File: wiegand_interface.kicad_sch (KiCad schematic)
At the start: 10 parts, among them U7 LTV-827S, U8 LTV-827S

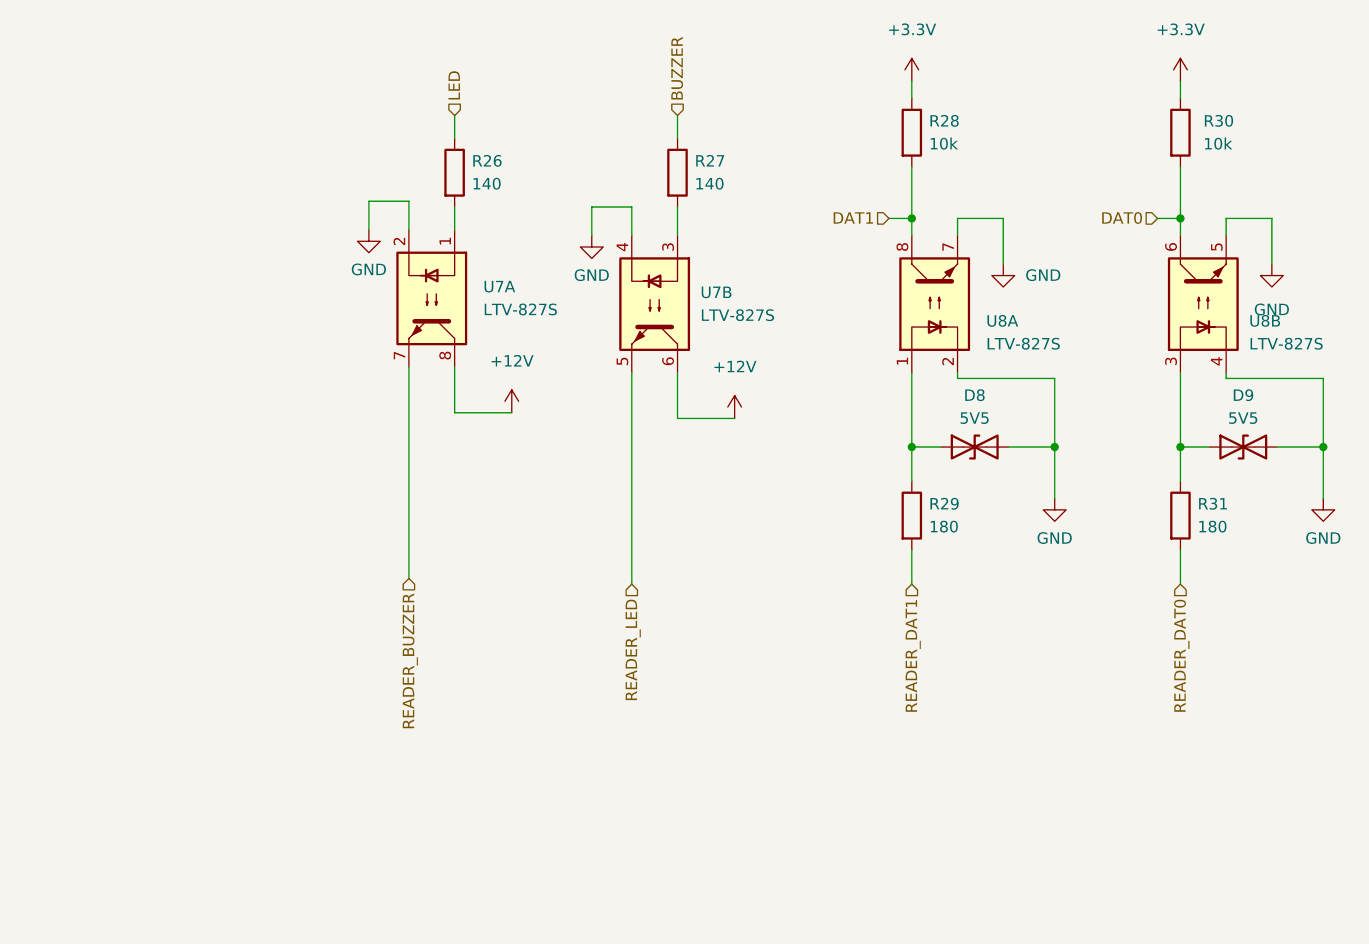
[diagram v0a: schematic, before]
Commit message: fix PoE transofrmer polarity, add more relay outputs
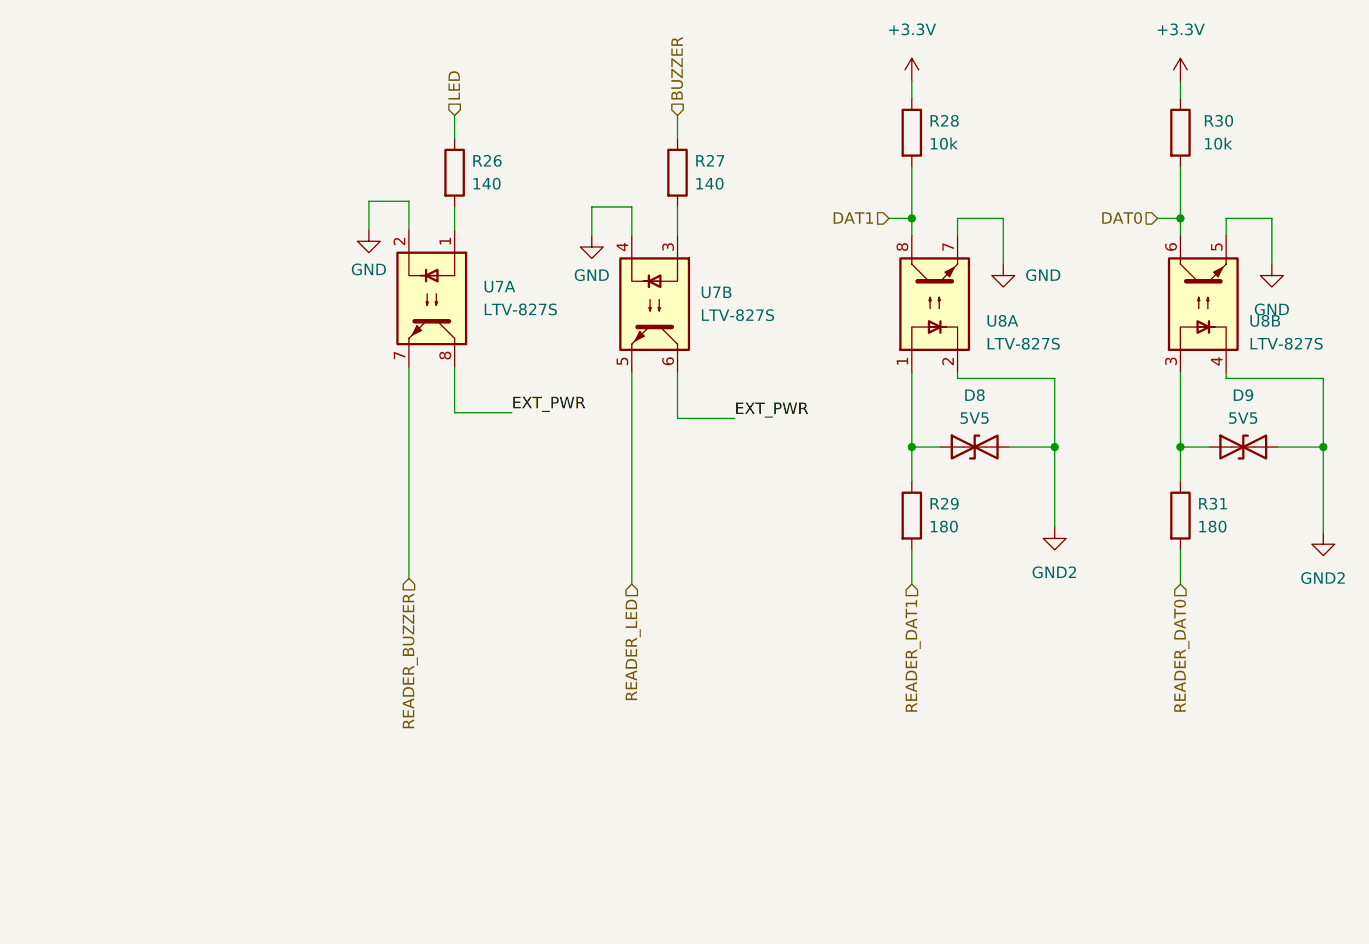
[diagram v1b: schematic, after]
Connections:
- net GND: no longer D8.2 (A2), D9.2 (A2), U8.2, U8.4
- net +12V renamed EXT_PWR
- new net GND2: D8.2 (A2), D9.2 (A2), U8.2, U8.4
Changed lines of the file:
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@@
+	(wire
+		(pts
+			(xy 160.02 114.3) (xy 160.02 123.19)
+		)
+		(stroke
+			(width 0)
+			(type default)
+		)
+	)
 	(wire
 		(pts
@@
 	(wire
 		(pts
-			(xy 160.02 120.015) (xy 160.02 114.3)
-		)
-		(stroke
-			(width 0)
-			(type default)
-		)
-	)
-	(wire
-		(pts
 			(xy 173.99 114.3) (xy 177.165 114.3)
 		)
@@
 	(wire
 		(pts
-			(xy 189.865 120.015) (xy 189.865 114.3)
+			(xy 189.865 114.3) (xy 189.865 123.825)
 		)
 		(stroke
@@
 			(width 0)
 			(type default)
+		)
+	)
+	(label "EXT_PWR"
+		(at 124.46 111.125 0)
+		(effects
+			(font
+				(size 1.27 1.27)
+			)
+			(justify left bottom)
+		)
+	)
+	(label "EXT_PWR"
+		(at 99.695 110.49 0)
+		(effects
+			(font
+				(size 1.27 1.27)
+			)
+			(justify left bottom)
 		)
 	)
@@
 	)
 	(symbol
-		(lib_id "power:GND")
-		(at 189.865 120.015 0)
-		(unit 1)
-		(exclude_from_sim no)
-		(in_bom yes)
-		(on_board yes)
-		(dnp no)
-		(fields_autoplaced yes)
-		(property "Reference" "#PWR064"
-			(at 189.865 126.365 0)
-			(effects
-				(font
-					(size 1.27 1.27)
-				)
-				(hide yes)
-			)
-		)
-		(property "Value" "GND"
-			(at 189.865 124.46 0)
-			(effects
-				(font
-					(size 1.27 1.27)
-				)
-			)
-		)
-		(property "Footprint" ""
-			(at 189.865 120.015 0)
-			(effects
-				(font
-					(size 1.27 1.27)
-				)
-				(hide yes)
-			)
-		)
-		(property "Datasheet" ""
-			(at 189.865 120.015 0)
-			(effects
-				(font
-					(size 1.27 1.27)
-				)
-				(hide yes)
-			)
-		)
-		(property "Description" ""
-			(at 189.865 120.015 0)
-			(effects
-				(font
-					(size 1.27 1.27)
-				)
-				(hide yes)
-			)
-		)
-		(pin "1"
-		)
-		(instances
-			(project ""
-				(path "/727d6c0a-a0ef-4feb-9656-3db3cb90564a/6b89ba24-3094-438d-a07a-020a470fc0fc"
-					(reference "#PWR064")
-					(unit 1)
-				)
-			)
-		)
-	)
-	(symbol
 		(lib_id "Device:R")
 		(at 93.345 83.82 0)
@@
 	)
 	(symbol
-		(lib_id "power:+12V")
-		(at 99.695 110.49 0)
+		(lib_id "power:GND2")
+		(at 189.865 123.825 0)
 		(unit 1)
 		(exclude_from_sim no)
@@
 		(dnp no)
 		(fields_autoplaced yes)
-		(property "Reference" "#PWR056"
-			(at 99.695 114.3 0)
-			(effects
-				(font
-					(size 1.27 1.27)
-				)
-				(hide yes)
-			)
-		)
-		(property "Value" "+12V"
-			(at 99.695 104.775 0)
+		(property "Reference" "#PWR07"
+			(at 189.865 130.175 0)
+			(effects
+				(font
+					(size 1.27 1.27)
+				)
+				(hide yes)
+			)
+		)
+		(property "Value" "GND2"
+			(at 189.865 128.905 0)
 			(effects
 				(font
@@
 		)
 		(property "Footprint" ""
-			(at 99.695 110.49 0)
+			(at 189.865 123.825 0)
 			(effects
 				(font
@@
 		)
 		(property "Datasheet" ""
-			(at 99.695 110.49 0)
-			(effects
-				(font
-					(size 1.27 1.27)
-				)
-				(hide yes)
-			)
-		)
-		(property "Description" ""
-			(at 99.695 110.49 0)
-			(effects
-				(font
-					(size 1.27 1.27)
-				)
-				(hide yes)
-			)
-		)
-		(pin "1"
-		)
-		(instances
-			(project ""
-				(path "/727d6c0a-a0ef-4feb-9656-3db3cb90564a/6b89ba24-3094-438d-a07a-020a470fc0fc"
-					(reference "#PWR056")
-					(unit 1)
-				)
-			)
-		)
-	)
-	(symbol
-		(lib_id "power:+12V")
-		(at 124.46 111.125 0)
-		(unit 1)
-		(exclude_from_sim no)
-		(in_bom yes)
-		(on_board yes)
-		(dnp no)
-		(fields_autoplaced yes)
-		(property "Reference" "#PWR058"
-			(at 124.46 114.935 0)
-			(effects
-				(font
-					(size 1.27 1.27)
-				)
-				(hide yes)
-			)
-		)
-		(property "Value" "+12V"
-			(at 124.46 105.41 0)
-			(effects
-				(font
-					(size 1.27 1.27)
-				)
-			)
-		)
-		(property "Footprint" ""
-			(at 124.46 111.125 0)
-			(effects
-				(font
-					(size 1.27 1.27)
-				)
-				(hide yes)
-			)
-		)
-		(property "Datasheet" ""
-			(at 124.46 111.125 0)
-			(effects
-				(font
-					(size 1.27 1.27)
-				)
-				(hide yes)
-			)
-		)
-		(property "Description" ""
-			(at 124.46 111.125 0)
-			(effects
-				(font
-					(size 1.27 1.27)
-				)
-				(hide yes)
-			)
-		)
-		(pin "1"
-		)
-		(instances
-			(project ""
-				(path "/727d6c0a-a0ef-4feb-9656-3db3cb90564a/6b89ba24-3094-438d-a07a-020a470fc0fc"
-					(reference "#PWR058")
+			(at 189.865 123.825 0)
+			(effects
+				(font
+					(size 1.27 1.27)
+				)
+				(hide yes)
+			)
+		)
+		(property "Description" "Power symbol creates a global label with name \"GND2\" , ground"
+			(at 189.865 123.825 0)
+			(effects
+				(font
+					(size 1.27 1.27)
+				)
+				(hide yes)
+			)
+		)
+		(pin "1"
+		)
+		(instances
+			(project "Zamkonator"
+				(path "/727d6c0a-a0ef-4feb-9656-3db3cb90564a/6b89ba24-3094-438d-a07a-020a470fc0fc"
+					(reference "#PWR07")
 					(unit 1)
 				)
@@
 	)
 	(symbol
+		(lib_id "power:GND2")
+		(at 160.02 123.19 0)
+		(unit 1)
+		(exclude_from_sim no)
+		(in_bom yes)
+		(on_board yes)
+		(dnp no)
+		(fields_autoplaced yes)
+		(property "Reference" "#PWR06"
+			(at 160.02 129.54 0)
+			(effects
+				(font
+					(size 1.27 1.27)
+				)
+				(hide yes)
+			)
+		)
+		(property "Value" "GND2"
+			(at 160.02 128.27 0)
+			(effects
+				(font
+					(size 1.27 1.27)
+				)
+			)
+		)
+		(property "Footprint" ""
+			(at 160.02 123.19 0)
+			(effects
+				(font
+					(size 1.27 1.27)
+				)
+				(hide yes)
+			)
+		)
+		(property "Datasheet" ""
+			(at 160.02 123.19 0)
+			(effects
+				(font
+					(size 1.27 1.27)
+				)
+				(hide yes)
+			)
+		)
+		(property "Description" "Power symbol creates a global label with name \"GND2\" , ground"
+			(at 160.02 123.19 0)
+			(effects
+				(font
+					(size 1.27 1.27)
+				)
+				(hide yes)
+			)
+		)
+		(pin "1"
+		)
+		(instances
+			(project ""
+				(path "/727d6c0a-a0ef-4feb-9656-3db3cb90564a/6b89ba24-3094-438d-a07a-020a470fc0fc"
+					(reference "#PWR06")
+					(unit 1)
+				)
+			)
+		)
+	)
+	(symbol
 		(lib_id "Device:R")
 		(at 173.99 79.375 0)
@@
 					(unit 1)
 				)
-			)
-		)
-	)
-	(symbol
-		(lib_id "power:GND")
-		(at 160.02 120.015 0)
-		(unit 1)
-		(exclude_from_sim no)
-		(in_bom yes)
-		(on_board yes)
-		(dnp no)
-		(fields_autoplaced yes)
-		(property "Reference" "#PWR061"
-			(at 160.02 126.365 0)
-			(effects
-				(font
-					(size 1.27 1.27)
-				)
-				(hide yes)
-			)
-		)
-		(property "Value" "GND"
-			(at 160.02 124.46 0)
-			(effects
-				(font
-					(size 1.27 1.27)
-				)
-			)
-		)
-		(property "Footprint" ""
-			(at 160.02 120.015 0)
-			(effects
-				(font
-					(size 1.27 1.27)
-				)
-				(hide yes)
-			)
-		)
-		(property "Datasheet" ""
-			(at 160.02 120.015 0)
-			(effects
-				(font
-					(size 1.27 1.27)
-				)
-				(hide yes)
-			)
-		)
-		(property "Description" ""
-			(at 160.02 120.015 0)
-			(effects
-				(font
-					(size 1.27 1.27)
-				)
-				(hide yes)
-			)
-		)
-		(pin "1"
-		)
-		(instances
-			(project ""
-				(path "/727d6c0a-a0ef-4feb-9656-3db3cb90564a/6b89ba24-3094-438d-a07a-020a470fc0fc"
-					(reference "#PWR061")
-					(unit 1)
-				)

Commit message: DO the bulk of rev 1.2 layout
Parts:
- removed U7, U8: LTV-827S, Package_DIP:SMDIP-8_W9.53mm, symbol Isolator:LTV-827S
- added D11, D12: PESD15VL1BA, Diode_SMD:D_SOD-323, symbol Device:D_TVS
- added U10, U7, U8, U9: EL3H7-G, project specific:SOIC127P700X200-4N, symbol EL3H7-G:EL3H7-G
- D8, D9: value 5V5 -> PESD5V0L1BA; footprint Diode_SMD:D_SMA-SMB_Universal_Handsoldering -> Diode_SMD:D_SOD-323; LCSC (none) -> C85380
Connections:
- net DAT0: now also U8.4
- net DAT1: now also U10.4
- net EXT_PWR: now also D11.1 (A1), D12.1 (A1), U7.4, U9.4
- net GND: now also U10.3, U7.2, U8.3, U9.2
- net GND2: now also D8.1 (A1), D9.1 (A1), U10.2, U8.2; no longer D8.2 (A2), D9.2 (A2)
- net READER_BUZZER: now also D11.2 (A2), U7.3
- net READER_LED: now also D12.2 (A2), U9.3
- net at R26.2: now also U9.1
- net at R27.2: now also U7.1
- net at R29.1: now also D8.2 (A2), U10.1; no longer D8.1 (A1)
- net at R31.1: now also D9.2 (A2), U8.1; no longer D9.1 (A1)
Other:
- moved on the sheet: D8, R26, R27, R28, R29, R30, R31

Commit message: Use kicad symbol for the optotransistor
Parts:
- U10, U7, U8, U9: footprint project specific:SOIC127P700X200-4N -> Package_SO:SSOP-4_4.4x2.6mm_P1.27mm
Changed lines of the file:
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@@
 			)
 		)
-		(property "Footprint" "project specific:SOIC127P700X200-4N"
+		(property "Footprint" "Package_SO:SSOP-4_4.4x2.6mm_P1.27mm"
 			(at 91.44 107.95 0)
 			(effects
@@
 			)
 		)
-		(property "Footprint" "project specific:SOIC127P700X200-4N"
+		(property "Footprint" "Package_SO:SSOP-4_4.4x2.6mm_P1.27mm"
 			(at 59.69 105.41 0)
 			(effects
@@
 			)
 		)
-		(property "Footprint" "project specific:SOIC127P700X200-4N"
+		(property "Footprint" "Package_SO:SSOP-4_4.4x2.6mm_P1.27mm"
 			(at 143.51 107.95 0)
 			(effects
@@
 			)
 		)
-		(property "Footprint" "project specific:SOIC127P700X200-4N"
+		(property "Footprint" "Package_SO:SSOP-4_4.4x2.6mm_P1.27mm"
 			(at 116.84 107.95 0)
 			(effects

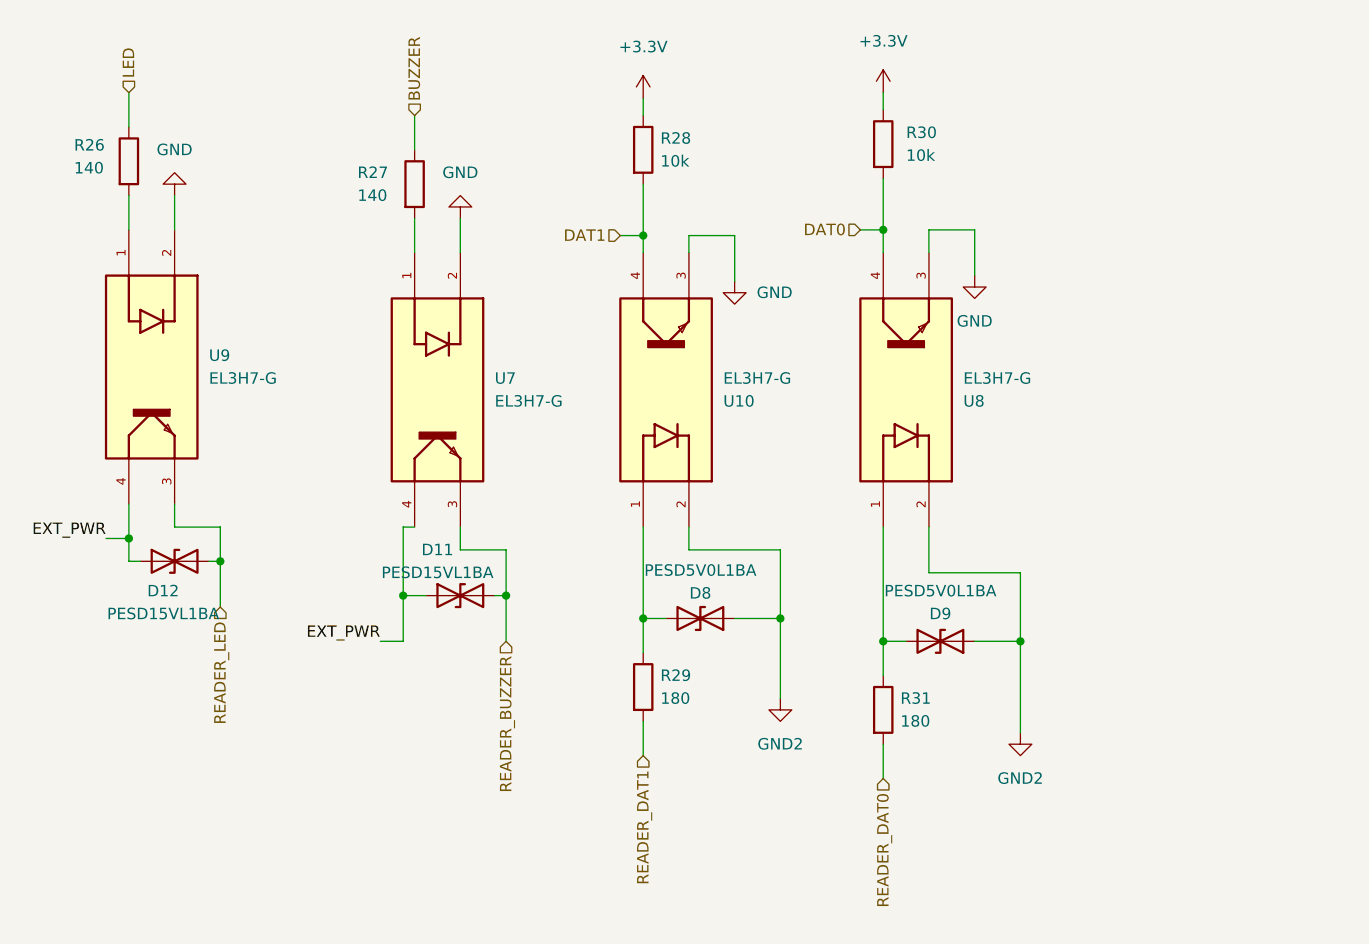
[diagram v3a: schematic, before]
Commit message: Remove custom library for EL3H7, use the kicad one.
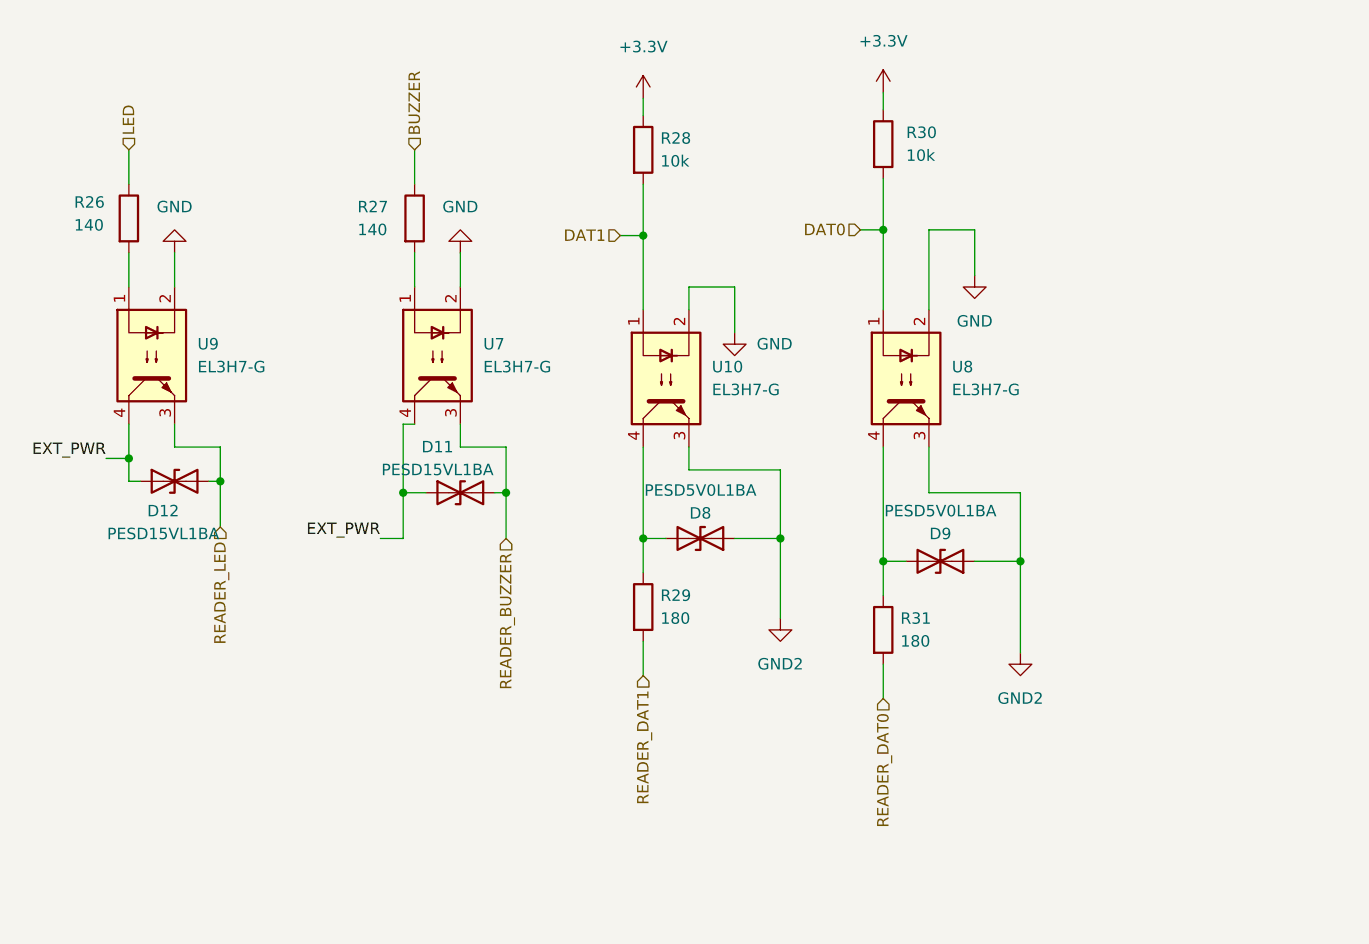
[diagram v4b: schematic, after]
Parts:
- removed U10, U7, U8, U9: EL3H7-G, Package_SO:SSOP-4_4.4x2.6mm_P1.27mm, symbol EL3H7-G:EL3H7-G
- added U10, U7, U8, U9: EL3H7-G, Package_SO:SSOP-4_4.4x2.6mm_P1.27mm, symbol Isolator:Optocoupler_DC_PhotoNPN_AKEC
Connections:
- net DAT0: now also U8.1
- net DAT1: now also U10.1
- net EXT_PWR: now also U7.4, U9.4
- net GND: now also U10.2, U7.2, U8.2, U9.2
- net GND2: now also U10.3, U8.3
- net READER_BUZZER: now also U7.3
- net READER_LED: now also U9.3
- net at R26.2: now also U9.1
- net at R27.2: now also U7.1
- net at D8.2 (A2), R29.1: now also U10.4
- net at D9.2 (A2), R31.1: now also U8.4
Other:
- moved on the sheet: D11, D12, D8, D9, R26, R27, R29, R31
